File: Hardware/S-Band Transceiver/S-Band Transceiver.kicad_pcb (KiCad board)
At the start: 4 copper layers, 171.4 x 101.6 mm, 216 parts, among them J1 SMA, J2 SMA, J3 AVR-UPDI-6, J4 USB_C_Receptacle_USB2.0_16P, J5 SMA, J6 SMA, J7 SMA, J8 SMA, SW1 SW_Push, U1 ADF4351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

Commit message: Routing board
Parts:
- moved C28 0.56 mm to (129.5, 65.3)
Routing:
- net SYNTH_TX: track 0.00 -> 65.9 mm
- net +3.3VA: track 5.84 -> 21.1 mm, vias 1 -> 6
- net Net-(U1-RF_OUT_A+): track 0.00 -> 8.98 mm
- net Net-(U1-RF_OUT_A-): track 0.00 -> 8.82 mm
- net Net-(U7-PUP2): track 0.00 -> 4.52 mm
- net Net-(U7-PUP1): track 0.00 -> 4.44 mm
- net Net-(U8-S/~{P}): track 0.00 -> 4.16 mm
- net TX_ATTEN_LE: track 0.00 -> 3.70 mm
- net Net-(U7-RFOUT): track 0.00 -> 3.52 mm
- net Net-(R28-Pad2): track 0.00 -> 3.30 mm
- net Net-(R27-Pad2): track 0.00 -> 3.24 mm
- net Net-(U8-RF1): track 0.00 -> 3.17 mm
- net Net-(U8-OPT): track 0.00 -> 3.03 mm
- net +5V: track 14.1 -> 15.5 mm, vias 2 -> 3

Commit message: Updating board layout and routing
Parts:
- added H1: 4-40, B12T_MountingHole:4-40_Hole_Pad, F.Cu at (67.3, 29.2)
- added H2: 4-40, B12T_MountingHole:4-40_Hole_Pad, F.Cu at (186.7, 29.2)
- added H3: 4-40, B12T_MountingHole:4-40_Hole_Pad, F.Cu at (67.3, 123.2)
- added H4: 4-40, B12T_MountingHole:4-40_Hole_Pad, F.Cu at (186.7, 123.2)
- added REF**: OSHW-Symbol_6.7x6mm_SilkScreen, Symbol:OSHW-Symbol_6.7x6mm_SilkScreen, F.Cu at (152.3, 31.1)
- R45: value 0 -> 10k
- moved J3 37.8 mm to (158.1, 121.3)
- moved D5 27.4 mm to (181.1, 122.5), turned to 90 degrees
- moved C1 23.3 mm to (154.4, 58.7), turned to 90 degrees
- moved R2 23.1 mm to (147.3, 61.8), turned to 180 degrees
- moved C48 23.0 mm to (174.2, 94.5), turned to -90 degrees
- moved R1 23.0 mm to (147.3, 59.1), turned to 180 degrees
- moved C46 22.9 mm to (163.5, 108.6)
- moved R22 22.9 mm to (160.0, 106.0)
- moved R24 22.9 mm to (160.0, 108.5)
- moved C40 22.5 mm to (136.7, 85.7)
- moved C41 22.5 mm to (136.7, 87.6)
- moved R13 22.5 mm to (140.1, 84.0)
- moved C39 22.5 mm to (136.7, 83.7)
- moved R14 22.5 mm to (140.1, 86.5)
- moved U3 22.5 mm to (138.9, 80.3)
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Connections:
- C42 pad 1: USBDP -> USBDM
- C43 pad 1: USBDM -> USBDP
- J6 pad 1: I_IF -> Q_IF
- J7 pad 1: Q_IF -> I_IF
- R18 pad 1: USBDM -> USBDP
- R19 pad 1: USBDP -> USBDM
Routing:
- net EXT_REF: track 0.00 -> 45.0 mm
- net Q_IF: track 0.00 -> 44.4 mm
- net I_IF: track 0.00 -> 43.9 mm
- net +3.3VA: track 21.1 -> 62.9 mm, vias 6 -> 13
- net Net-(U1-VTUNE): track 0.00 -> 21.9 mm, vias 0 -> 2
- net VBUS: track 0.00 -> 15.7 mm
- net +5V: track 15.5 -> 29.6 mm, vias 3 -> 6
- net LO+: track 0.00 -> 13.8 mm
- net LO-: track 0.00 -> 13.7 mm
- net GND: track 0.00 -> 13.2 mm, vias 0 -> 6
- net Net-(U1-SW): track 0.00 -> 12.6 mm, vias 0 -> 2
- net USBDP: track 0.00 -> 10.6 mm
- net USBDM: track 0.00 -> 10.4 mm
- net Net-(R53-Pad2): track 0.00 -> 8.61 mm
- net Net-(U1-CPout): track 0.00 -> 8.58 mm
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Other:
- board size 171.4 x 101.6 mm -> 127 x 101.6 mm
- board text added: "${TITLE} ${REVISION} ${COMMENT1}"
- board text added: "AUX OUT"
- board text added: "IF-I OUT"
- board text added: "IF-Q OUT"
- board text added: "RX IN"
- board text added: "TX OUT"

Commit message: Routing board
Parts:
- moved R22 21.9 mm to (178.0, 118.5), turned to -90 degrees
- moved C46 5.36 mm to (166.3, 104.0), turned to -90 degrees
- moved D6 2.80 mm to (180.8, 122.3)
- moved D2 2.80 mm to (171.8, 122.3)
- moved D5 2.80 mm to (178.3, 122.5)
- moved D3 2.80 mm to (174.9, 122.3)
- moved C44 2.09 mm to (171.7, 98.4)
- moved X1 0.11 mm to (151.8, 58.3)
- moved C1 0.11 mm to (154.4, 58.6)
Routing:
- net XO_REF: track 0.00 -> 2.56 mm
- net Net-(D1-A): track 0.00 -> 1.74 mm
- net +3.3VA: track 62.9 -> 64.5 mm
- net GND: vias 6 -> 7
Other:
- board text added: "Lock-Detect"

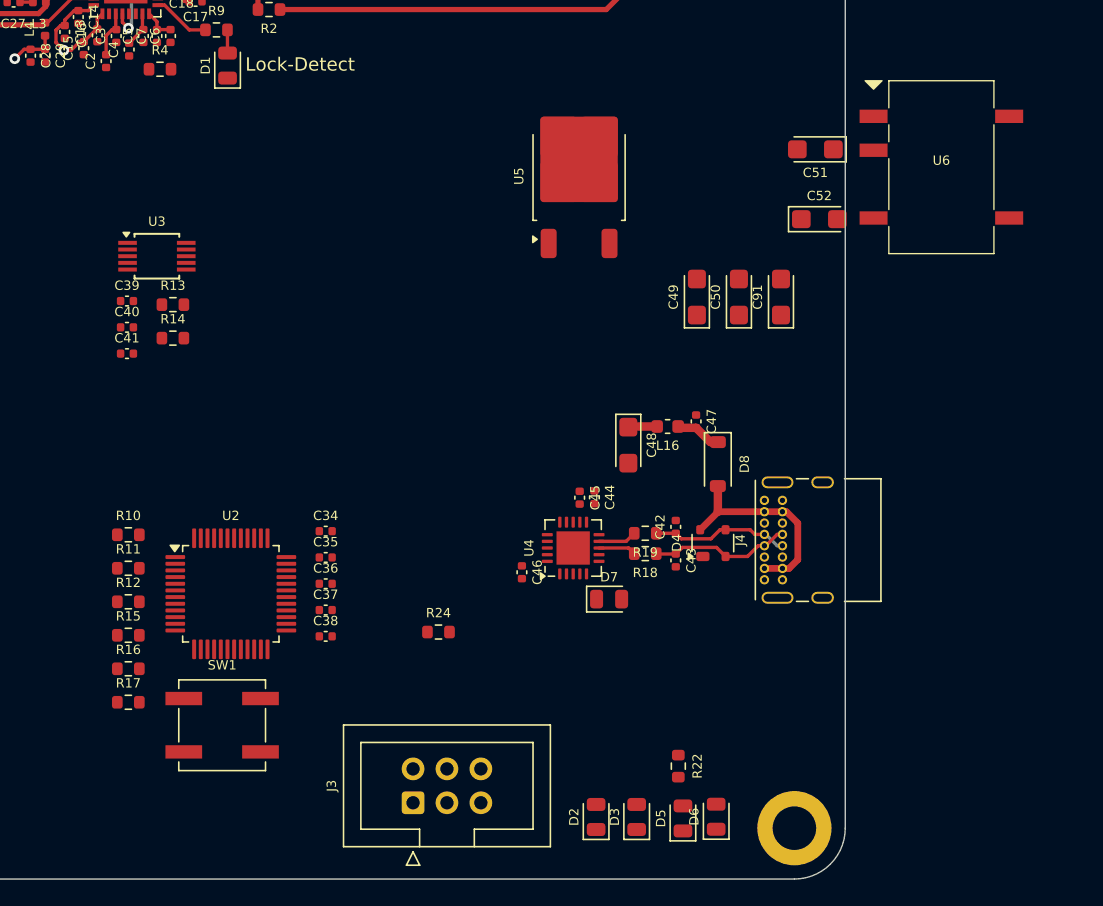
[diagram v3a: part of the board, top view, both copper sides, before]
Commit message: Routing microcontroller
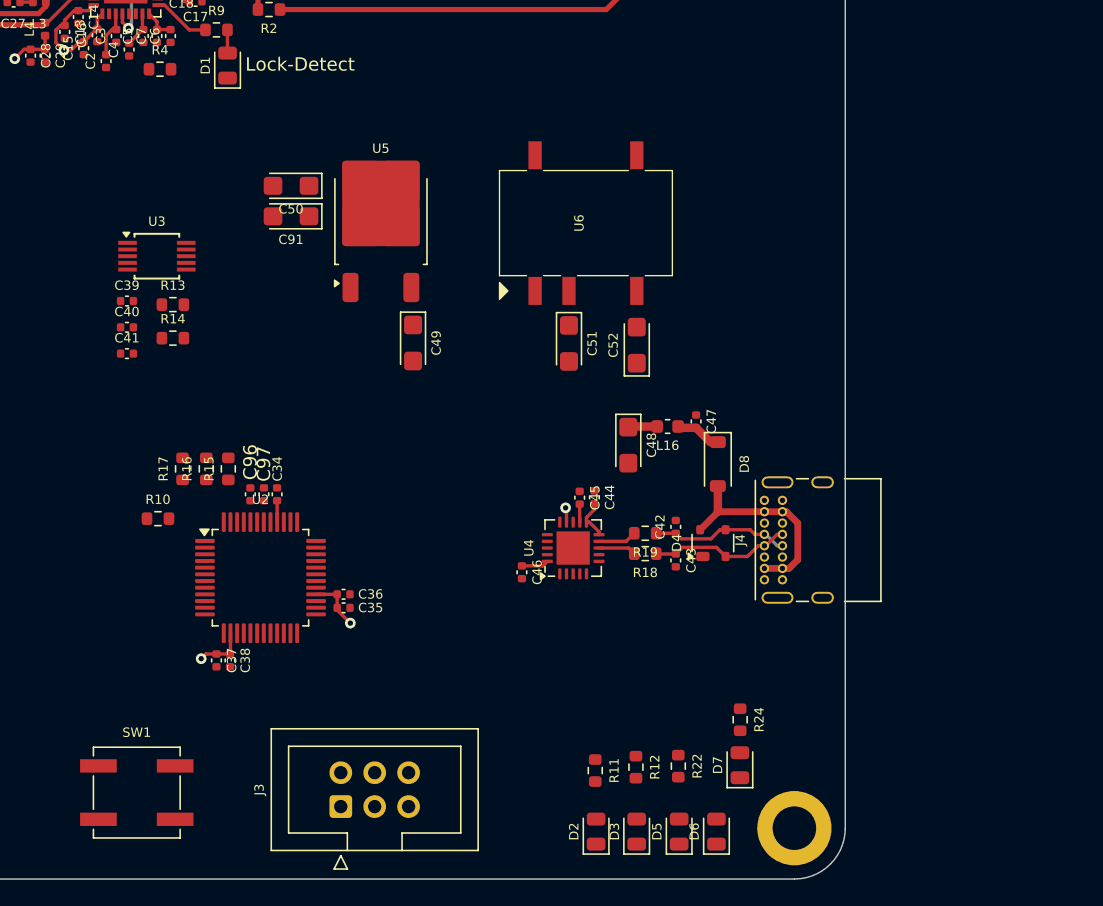
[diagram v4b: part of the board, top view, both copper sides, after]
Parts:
- added C96: 100nF, Capacitor_SMD:C_0402_1005Metric, F.Cu at (145.9, 98.2)
- added C97: 10nF, Capacitor_SMD:C_0402_1005Metric, F.Cu at (146.9, 98.2)
- moved R12 40.0 mm to (174.8, 118.6), turned to -90 degrees
- moved R11 38.1 mm to (171.8, 118.9), turned to -90 degrees
- moved C91 37.2 mm to (149.0, 77.3), turned to 180 degrees
- moved C50 34.6 mm to (149.0, 75.1), turned to 180 degrees
- moved U6 27.0 mm to (171.1, 77.9), turned to 90 degrees
- moved R24 23.5 mm to (182.6, 115.1), turned to -90 degrees
- moved C51 23.5 mm to (169.8, 86.9), turned to -90 degrees
- moved C49 21.5 mm to (158.1, 86.8), turned to -90 degrees
- moved R17 18.0 mm to (140.8, 96.3), turned to 90 degrees
- moved C52 16.6 mm to (174.9, 87.0), turned to 90 degrees
- moved R16 16.1 mm to (142.6, 96.3), turned to 90 degrees
- moved D7 15.8 mm to (182.6, 118.5), turned to 90 degrees
- moved U5 15.2 mm to (155.7, 77.6)
- moved R15 14.5 mm to (144.3, 96.3), turned to 90 degrees
- moved C37 9.01 mm to (143.4, 110.6), turned to -90 degrees
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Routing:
- net +3V3: track 0.00 -> 13.2 mm, vias 0 -> 2
- net Net-(U2-~{RESET}/PF6): track 0.00 -> 1.61 mm
- net +5V: track 29.6 -> 30.9 mm
- net RX_LED: track 0.00 -> 1.10 mm, vias 0 -> 1

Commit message: Updating routing
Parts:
- moved C67 274.8 mm to (77.2, 101.6), turned to 90 degrees
- moved R23 203.4 mm to (180.8, 117.3), turned to -90 degrees
- moved R21 202.3 mm to (179.8, 108.2), turned to 180 degrees
- moved R20 192.2 mm to (179.8, 106.2), turned to 180 degrees
- moved SW1 20.6 mm to (158.0, 121.1), turned to 180 degrees
- moved J3 12.8 mm to (140.0, 121.2)
- moved R10 11.1 mm to (149.5, 96.4), turned to -90 degrees
- moved D7 6.07 mm to (177.3, 121.4)
- moved R24 5.80 mm to (177.3, 117.3)
- moved D2 5.59 mm to (166.6, 121.4)
- moved R11 5.37 mm to (166.6, 117.3)
- moved D3 5.11 mm to (170.2, 121.4)
- moved R12 4.81 mm to (170.2, 117.3)
- moved D5 4.77 mm to (173.7, 121.4)
- moved R22 4.42 mm to (173.7, 117.3)
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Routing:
- net MOSI: track 4.32 -> 120.7 mm, vias 1 -> 4
- net SCLK: track 4.38 -> 117.0 mm, vias 1 -> 4
- net TX_AMP_EN: track 0.00 -> 66.8 mm
- net ~{SYNTH_CS}: track 3.87 -> 63.7 mm, vias 1 -> 2
- net C8: track 0.00 -> 54.3 mm
- net C4: track 0.00 -> 52.4 mm
- net C2: track 0.00 -> 51.6 mm
- net C1: track 0.00 -> 50.6 mm
- net C16: track 0.00 -> 48.9 mm, vias 0 -> 2
- net TX: track 5.18 -> 45.4 mm, vias 0 -> 2
- net RX: track 0.00 -> 35.5 mm, vias 0 -> 2
- net Net-(R10-Pad1): track 0.00 -> 34.8 mm, vias 0 -> 2
- net UPDI: track 0.00 -> 29.8 mm, vias 0 -> 2
- net MISO: track 0.00 -> 17.2 mm, vias 0 -> 2
- net Net-(J4-CC2): track 0.00 -> 14.9 mm, vias 0 -> 1
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- added copper zone on In2.Cu, net +3V3
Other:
- board text added: "+5V"
- board text added: "ERR"
- board text added: "RUN"
- board text added: "RX"
- board text added: "TX"

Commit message: Updating routing
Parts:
- added R66: 10k, Resistor_SMD:R_0603_1608Metric, F.Cu at (143.4, 64.6)
- moved C41 9.78 mm to (143.3, 80.4), turned to 180 degrees
- moved R14 9.14 mm to (131.8, 82.7)
- moved R13 8.96 mm to (131.7, 80.8)
- moved C40 5.90 mm to (134.1, 80.3), turned to 90 degrees
- moved D1 4.12 mm to (148.2, 67.1)
- moved R9 3.30 mm to (143.4, 66.7)
- moved C39 2.55 mm to (134.2, 83.2), turned to -90 degrees
- moved C67 0.19 mm to (77.4, 101.5)
- moved C49 0.13 mm to (158.0, 86.8)
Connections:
- C41 pad 2: +3V3 -> +3.3VA
- C70 pad 2: TX -> TX OUT
- J5 pad 1: TX -> TX OUT
- R3 pad 1: SYNTH_EN -> Net-(U1-CE)
- R45 pad 2: IQ_MIXER_EN -> Net-(U15-~{EN})
- U1 pad 26: PDB_RF -> Net-(U1-PDB_RF)
- U1 pad 4: SYNTH_EN -> Net-(U1-CE)
- U15 pad 7: IQ_MIXER_EN -> Net-(U15-~{EN})
- U2 pad 16: PDB_RF -> unconnected-(U2-PC4-Pad16)
- U2 pad 17: XO_EN -> RX_AMP_EN
- U2 pad 18: RX_AMP_EN -> XO_EN
- U2 pad 19: IQ_MIXER_EN -> unconnected-(U2-PC7-Pad19)
- U2 pad 33: SYNTH_EN -> unconnected-(U2-PE3-Pad33)
- U3 pad 8: +3V3 -> +3.3VA
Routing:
- net +5V: track 32.7 -> 341.2 mm, vias 7 -> 18
- net RX_AMP_EN: track 0.00 -> 131.2 mm, vias 0 -> 2
- net -5V: track 2.93 -> 129.6 mm, vias 0 -> 3
- net TX_VRMS: track 0.00 -> 73.7 mm, vias 0 -> 2
- net RX_VRMS: track 0.65 -> 73.9 mm, vias 0 -> 2
- net TX_PHASE_LE: track 0.00 -> 68.9 mm, vias 0 -> 2
- net XO_EN: track 0.00 -> 61.4 mm, vias 0 -> 2
- net LD: track 4.34 -> 51.2 mm, vias 0 -> 2
- net ~{CS_ADC}: track 0.00 -> 44.7 mm, vias 0 -> 2
- net GND: track 13.2 -> 53.5 mm, vias 7 -> 108
- net TX_ATTEN_LE: track 3.70 -> 40.3 mm, vias 0 -> 2
- net +3.3VA: track 64.5 -> 97.0 mm, vias 13 -> 40
- net RX_LED: track 1.62 -> 30.4 mm, vias 1 -> 2
- net ERROR_LED: track 0.00 -> 24.7 mm
- net TX_LED: track 0.00 -> 22.1 mm
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- added copper zone on In2.Cu, net +3.3VA
- added copper zone on B.Cu, net GND
- added copper zone on F.Cu, net GND
- added copper zone on In1.Cu, net GND

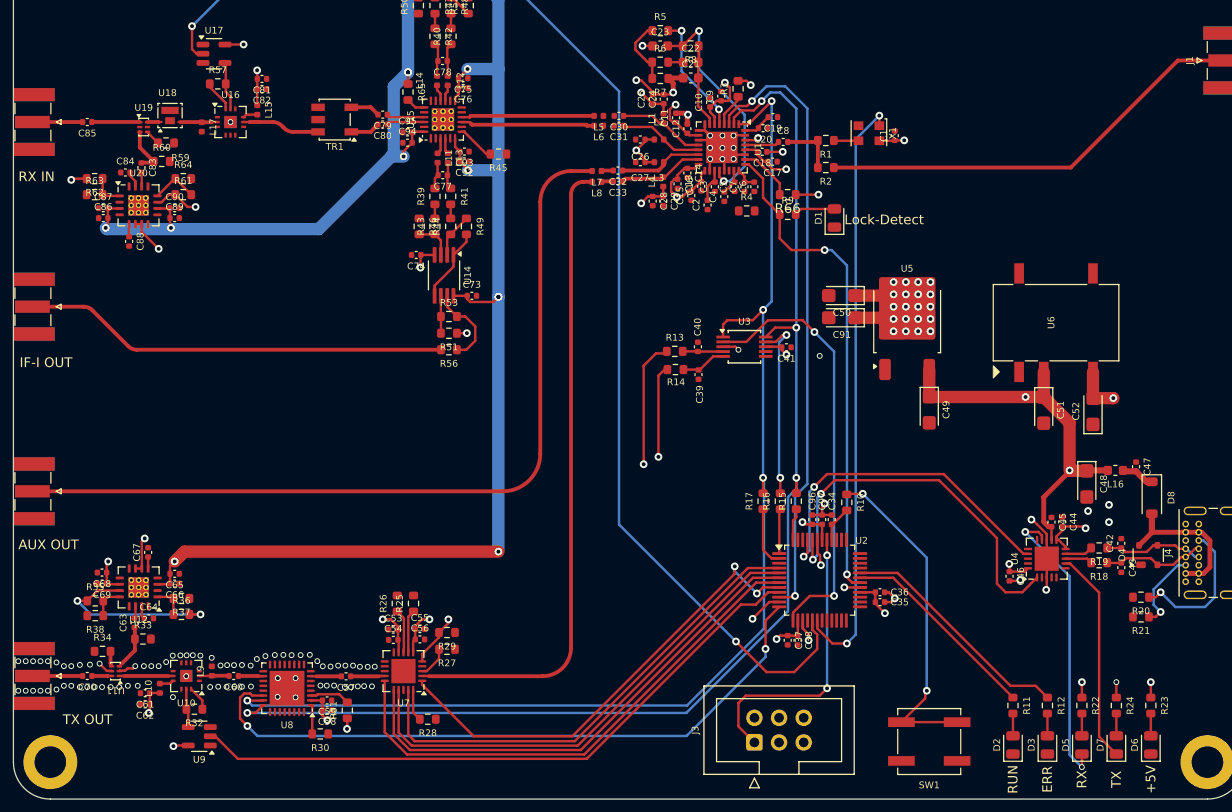
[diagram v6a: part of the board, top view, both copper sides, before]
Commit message: Updating silkscreen
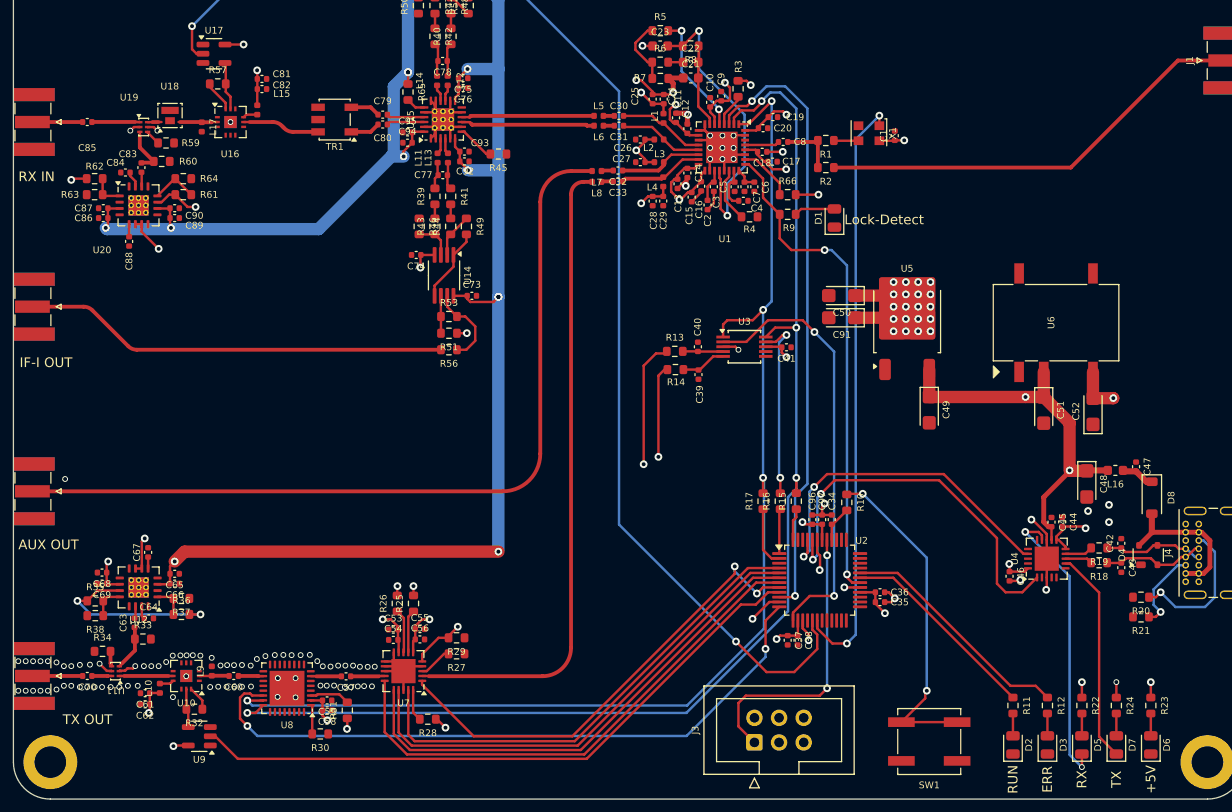
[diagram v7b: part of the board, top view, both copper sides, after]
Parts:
- moved C4 2.02 mm to (138.8, 65.3), turned to 180 degrees
- moved R29 1.13 mm to (109.2, 110.4)
- moved R27 1.09 mm to (109.2, 112.0)
- moved R4 0.68 mm to (139.4, 66.9)
- moved C15 0.16 mm to (133.5, 64.9)
- moved C3 0.11 mm to (135.8, 63.8)
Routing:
- net GND: track 53.5 -> 86.8 mm, vias 108 -> 113
- net Net-(U1-VTUNE): track 23.8 -> 30.6 mm
- net Net-(U1-RSET): track 0.00 -> 5.64 mm
- net +3.3VA: track 97.0 -> 93.1 mm, vias 40 -> 42
- net Net-(U1-VCOM): track 2.70 -> 4.38 mm
- net MUXOUT: track 1.44 -> 0.00 mm, vias 1 -> 0
- net Net-(C31-Pad2): track 0.00 -> 1.12 mm
- net Net-(C30-Pad2): track 0.00 -> 1.12 mm
- net Net-(U16-RF_OUT): track 8.99 -> 7.98 mm

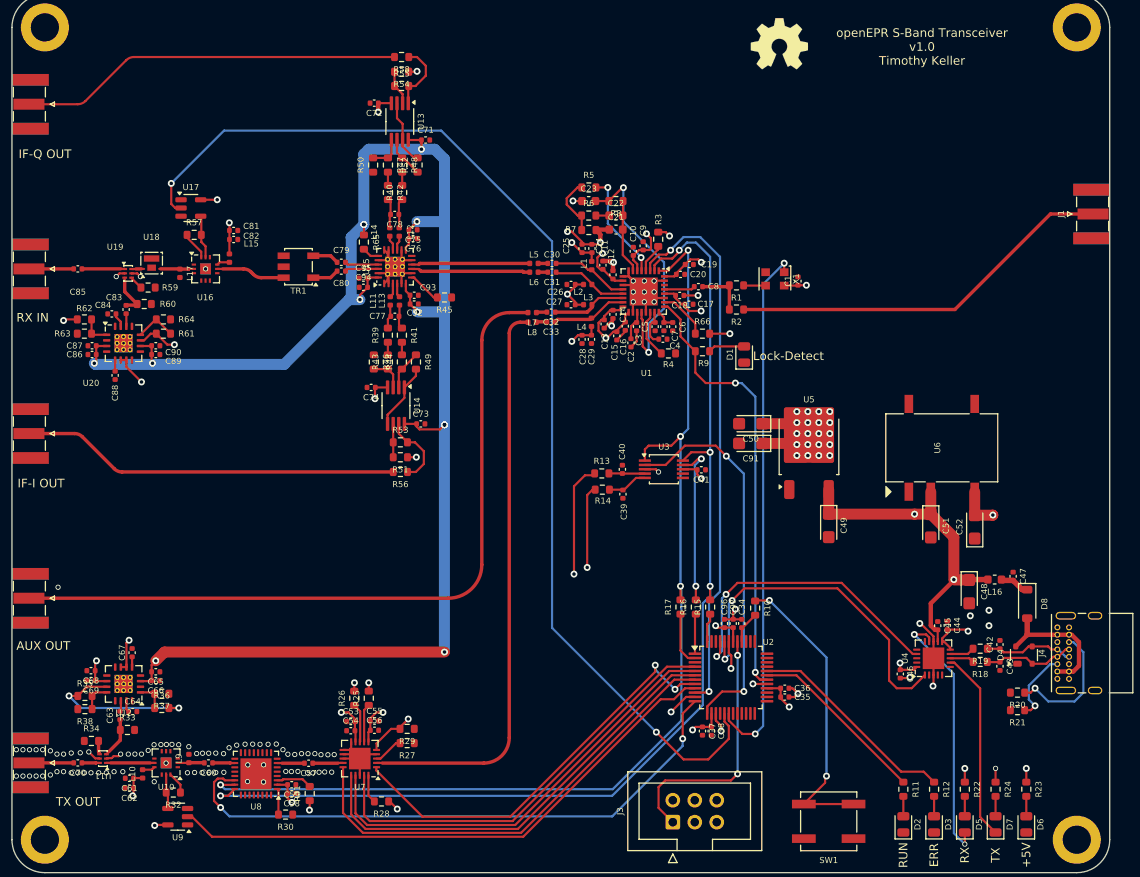
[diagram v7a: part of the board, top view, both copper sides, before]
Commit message: Cleaning up silkscreen
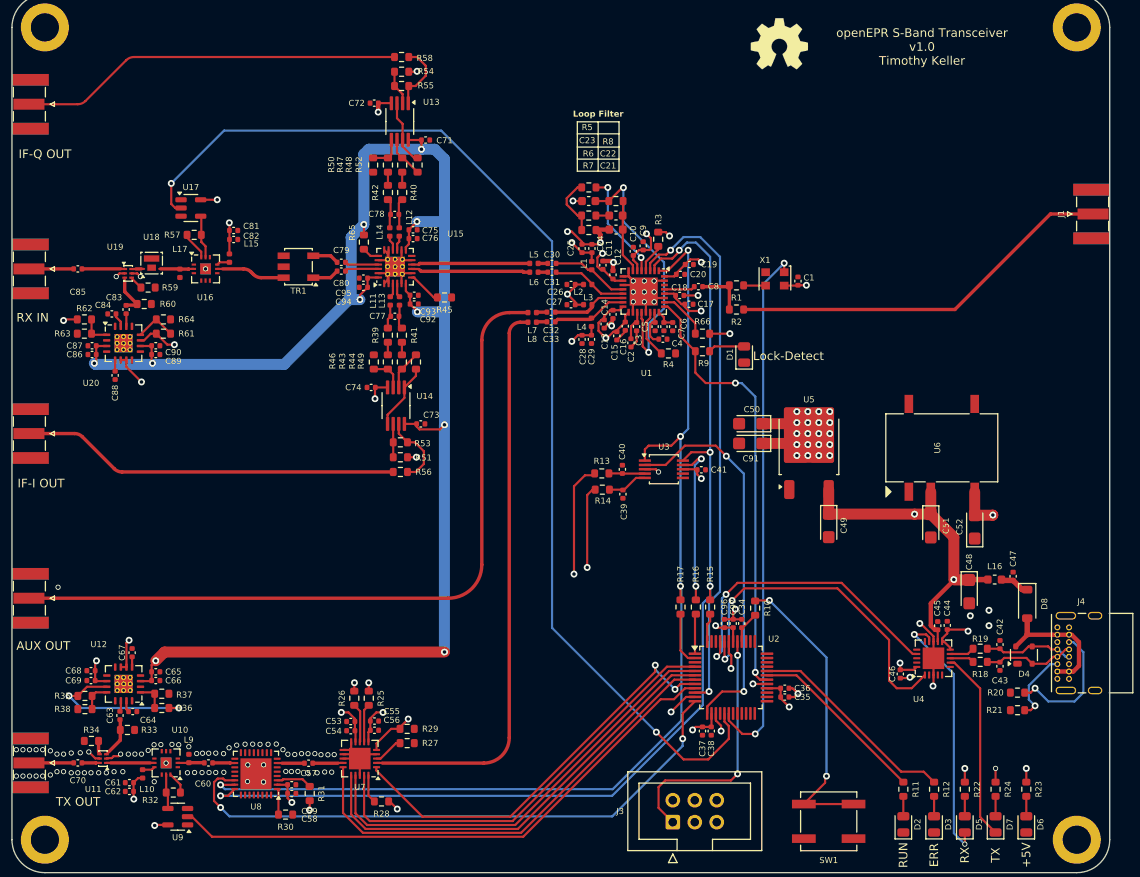
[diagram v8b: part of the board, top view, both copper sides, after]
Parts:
- moved C61 0.51 mm to (77.1, 116.6)
- moved C62 0.38 mm to (77.1, 117.6)
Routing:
- net GND: vias 113 -> 111
- net +5V: vias 18 -> 16
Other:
- board text added: "Loop Filter"
